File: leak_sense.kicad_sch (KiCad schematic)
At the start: 18 parts, among them J1 Conn_01x02, J2 Conn_01x02, J3 Conn_01x02, J4 Conn_01x02, J5 Conn_01x02

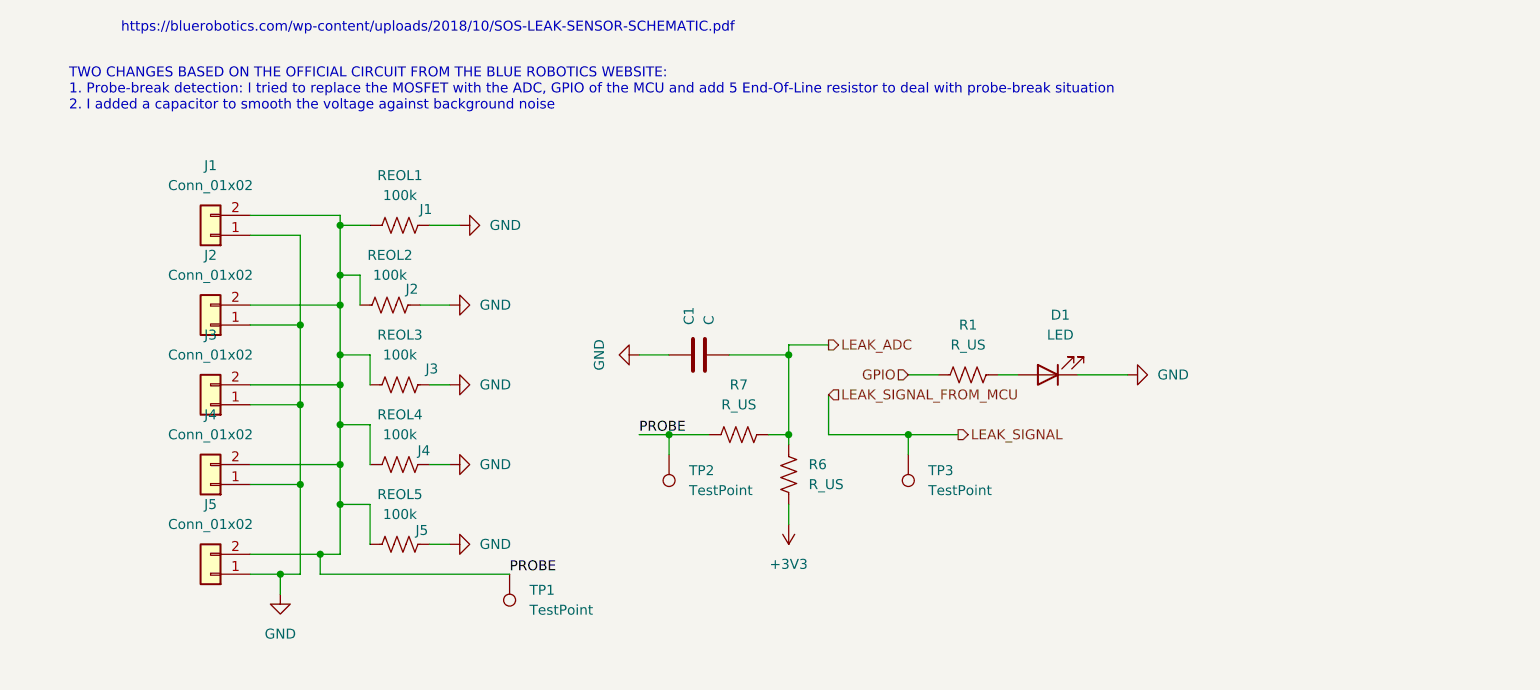
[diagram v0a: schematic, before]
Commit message: use the MOSFET instead, remove the EOL resistors
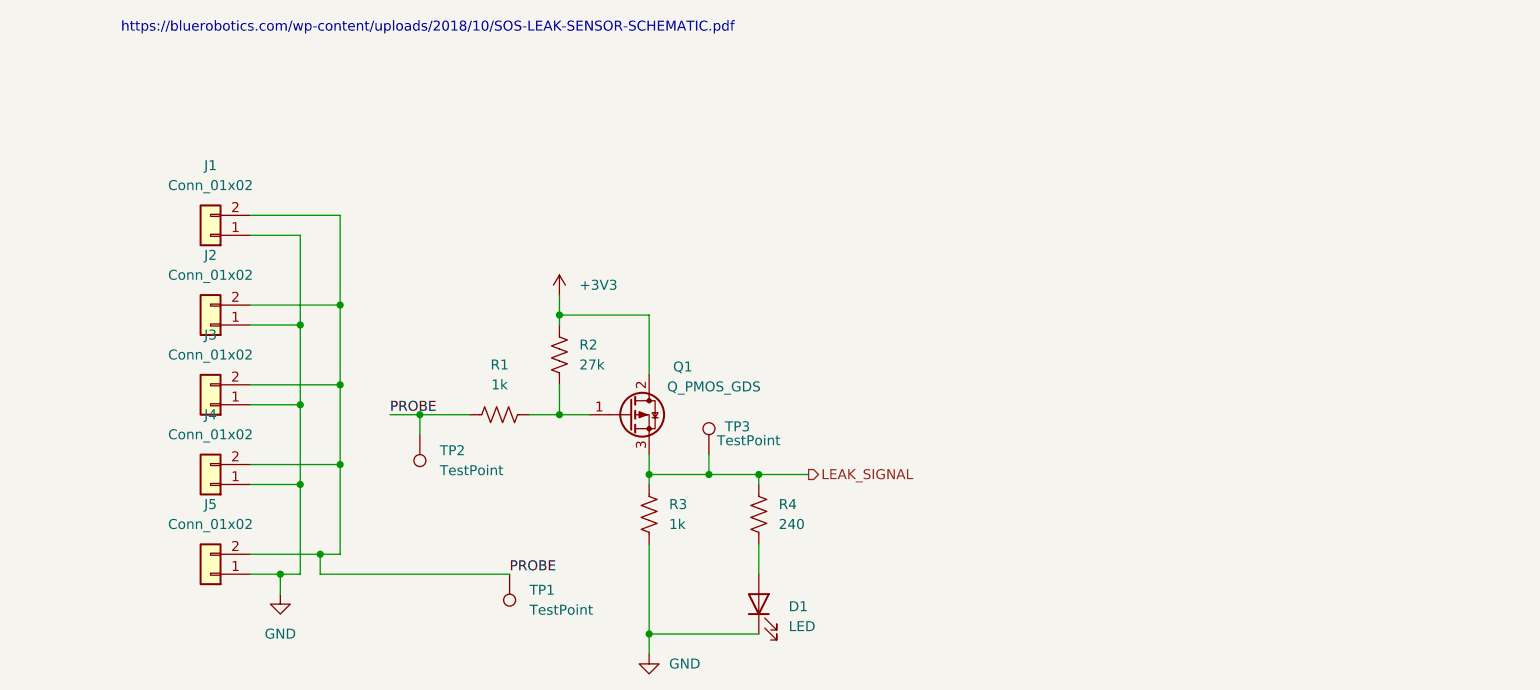
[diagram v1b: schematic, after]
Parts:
- removed C1: C, Package_SO:SOIC-8_3.9x4.9mm_P1.27mm, symbol Device:C
- removed R6, R7: R_US, symbol Device:R_US
- removed REOL1, REOL2, REOL3, REOL4, REOL5: 100k, symbol Device:R_US
- added Q1: Q_PMOS_GDS, Package_TO_SOT_SMD:TO-252-2, symbol Transistor_FET:Q_PMOS_GDS
- added R2: 27k, Package_TO_SOT_SMD:TO-252-2, symbol Device:R_US
- added R3: 1k, Package_TO_SOT_SMD:TO-252-2, symbol Device:R_US
- added R4: 240, Package_TO_SOT_SMD:TO-252-2, symbol Device:R_US
- R1: value R_US -> 1k; footprint (none) -> Package_TO_SOT_SMD:TO-252-2
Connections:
- net GPIO is gone; now on net PROBE: R1.1
- net +3V3: now also Q1.2 (D), R2.1
- net GND: now also R3.2
- net LEAK_SIGNAL: now also Q1.3 (S), R3.1, R4.1
- net at D1.2 (A): now also R4.2; no longer R1.2
- new net: Q1.1 (G), R1.2, R2.2
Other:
- note removed: "TWO CHANGES BASED ON THE OFFICIAL CIRCUIT FROM THE BLUE ROBOTICS WEBSITE: 1. Probe-break detection: I tried to replace the MOSFET with the ADC, GPIO of the MCU and add 5 End-Of-Line resistor to deal with probe-break situation 2. I added a capacitor to smooth the voltage against background noise"
- moved on the sheet: D1, TP2, TP3
